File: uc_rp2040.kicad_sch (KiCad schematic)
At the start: 39 parts, among them Q6 BC817-25W, SW2 SW_B3U-1000P_SMD, SW3 SW_B3U-1000P_SMD, U8 W25Q128JVSIQ_SOIC-8, U9 RP2040

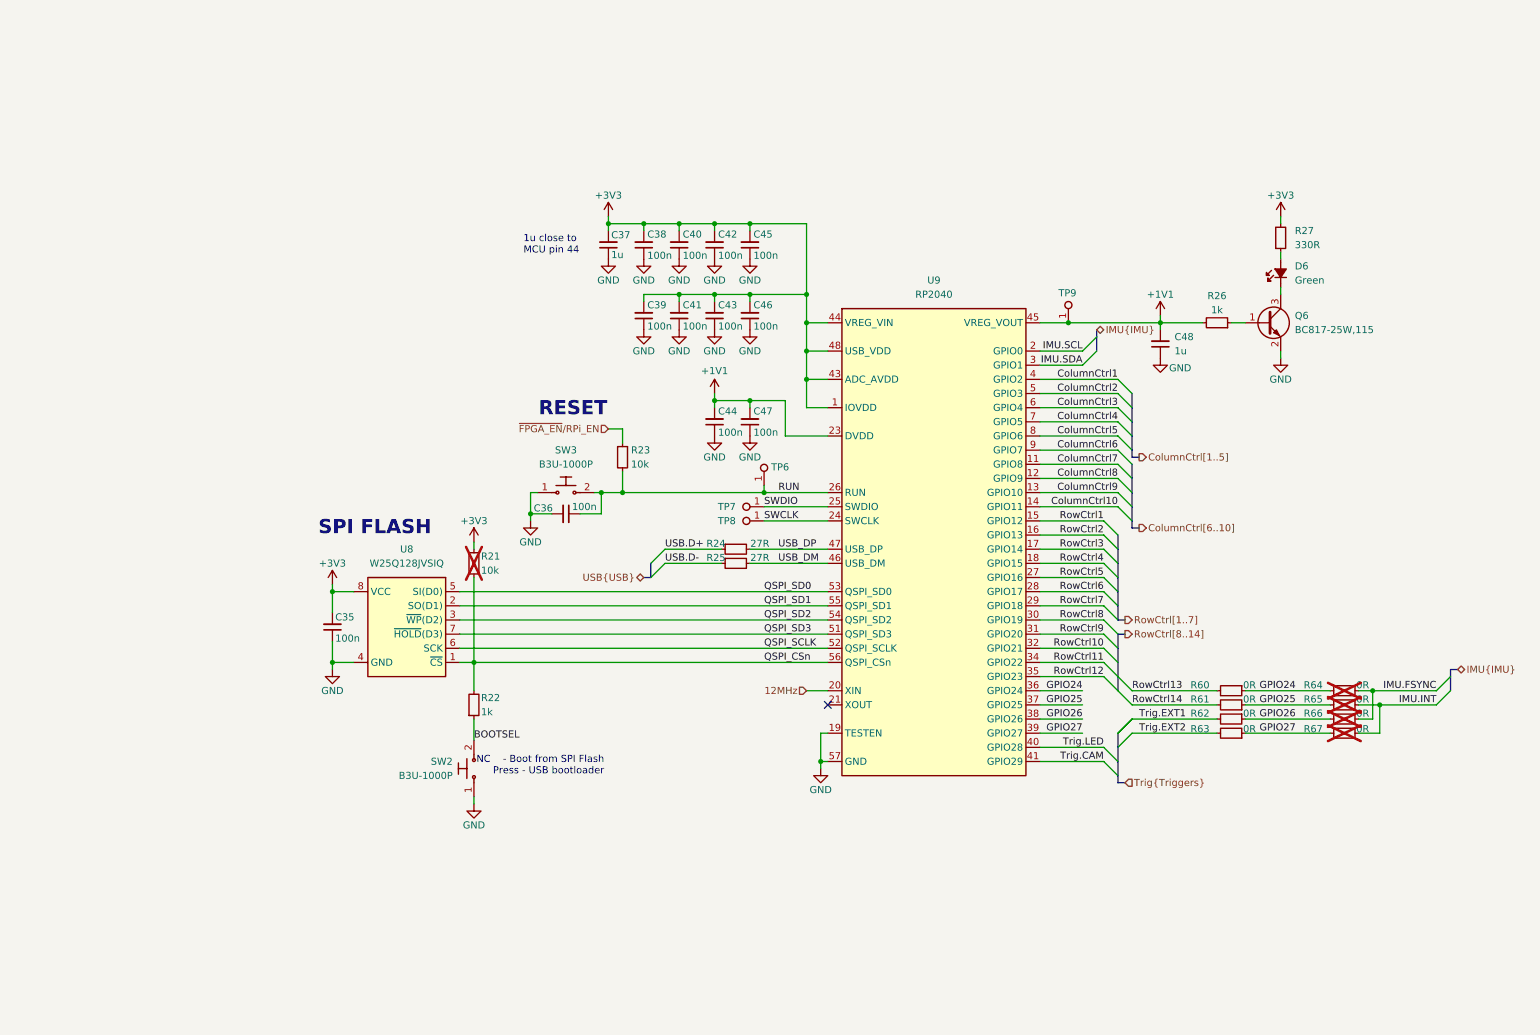
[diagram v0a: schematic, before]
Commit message: [#72133] Sch: Update control hierarchy
Signed-off-by: Dawid Lentka <dlentka@antmicro.com>
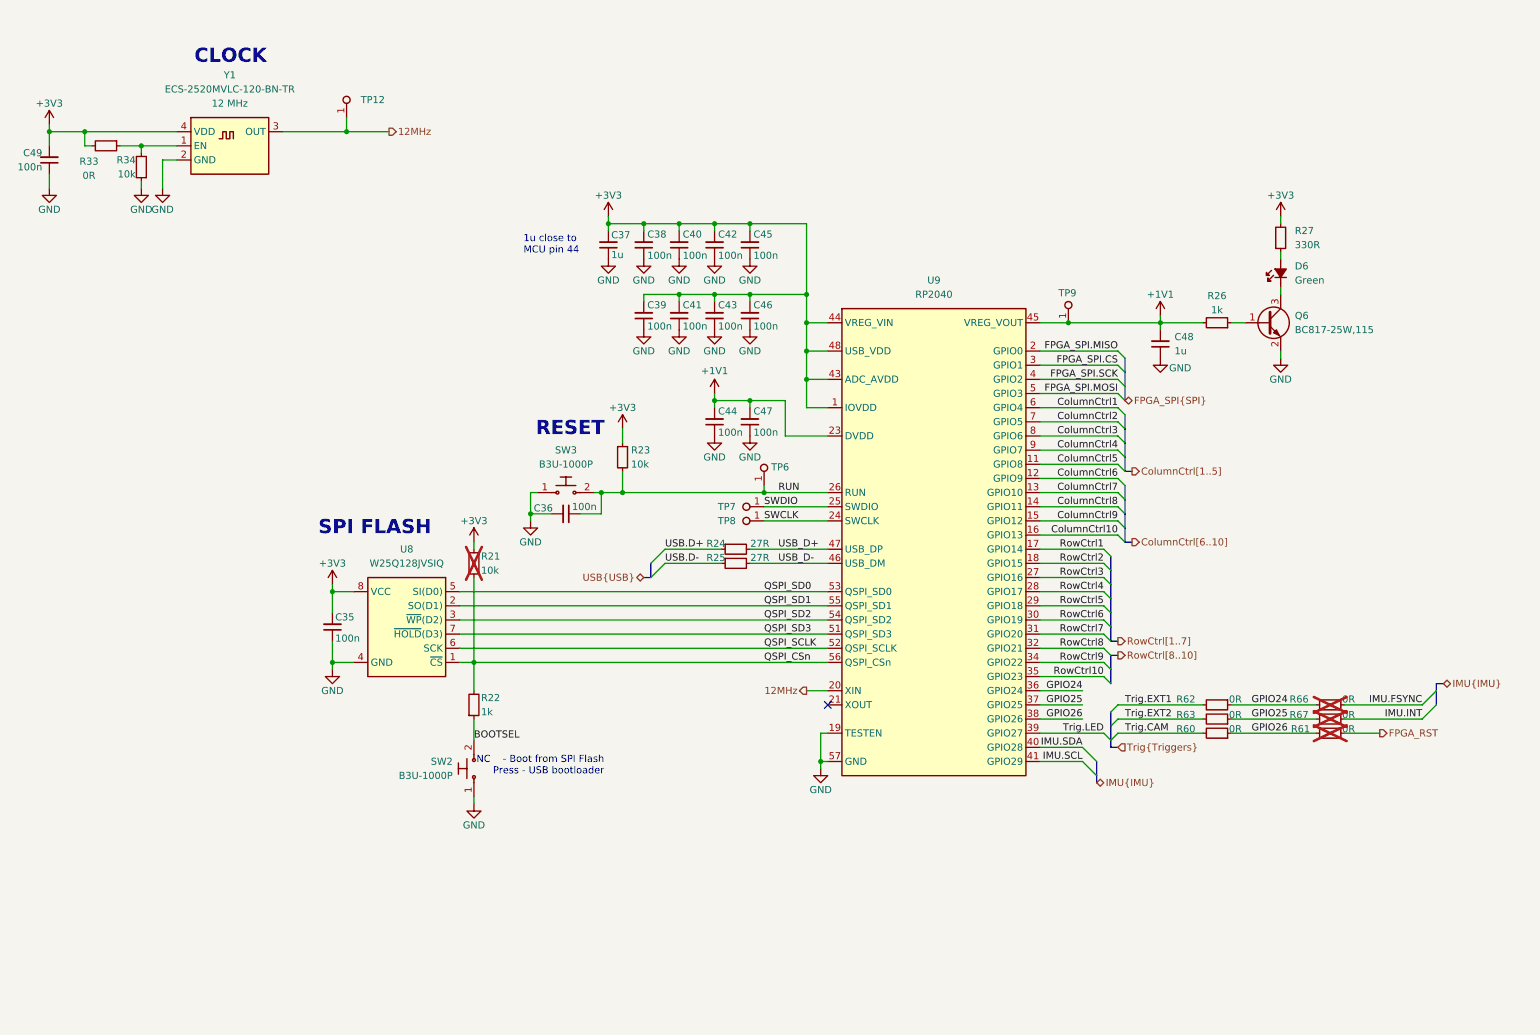
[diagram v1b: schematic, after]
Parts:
- removed R64, R65: R_0R_0402, antmicro-footprints:R_0402_1005Metric, symbol antmicroResistors0402:R_0R_0402
- added C49: C_100n_0402, antmicro-footprints:C_0402_1005Metric, symbol antmicroCapacitors0402:C_100n_0402
- added R33: R_0R_0402, antmicro-footprints:R_0402_1005Metric, symbol antmicroResistors0402:R_0R_0402
- added R34: R_10k_0402, antmicro-footprints:R_0402_1005Metric, symbol antmicroResistors0402:R_10k_0402
- added TP12: TP_0.75mm_SMD, antmicro-footprints:TP_SMD_0.75mm, symbol antmicroTestPoints:TP_0.75mm_SMD
- added Y1: Oscillator_12MHz_ESC_2520MV, antmicro-footprints:Oscillator_SMD_ECS_2520MV_2.5x2mm, symbol antmicroOscillators:Oscillator_12MHz_ESC_2520MV
- R61: now not fitted
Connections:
- net RowCtrl11 is gone; now on net RowCtrl9: U9.34 (GPIO22)
- net RowCtrl12 is gone; now on net RowCtrl10: U9.35 (GPIO23)
- net RowCtrl13 is gone; now on net Trig.CAM: R60.2
- net RowCtrl14 is gone; now on net GPIO26: R61.2
- net ~{FPGA_EN}/RPi_EN is gone; now on net +3V3: R23.1
- net +3V3: now also C49.2, R33.2, Y1.4 (VDD)
- net 12MHz: now also TP12.1, Y1.3 (OUT)
- net ColumnCtrl1: now also U9.6 (GPIO4); no longer U9.4 (GPIO2)
- net ColumnCtrl10: now also U9.16 (GPIO13); no longer U9.14 (GPIO11)
- net ColumnCtrl2: now also U9.7 (GPIO5); no longer U9.5 (GPIO3)
- net ColumnCtrl3: now also U9.8 (GPIO6); no longer U9.6 (GPIO4)
- net ColumnCtrl4: now also U9.9 (GPIO7); no longer U9.7 (GPIO5)
- net ColumnCtrl5: now also U9.11 (GPIO8); no longer U9.8 (GPIO6)
- net ColumnCtrl6: now also U9.12 (GPIO9); no longer U9.9 (GPIO7)
- net ColumnCtrl7: now also U9.13 (GPIO10); no longer U9.11 (GPIO8)
- net ColumnCtrl8: now also U9.14 (GPIO11); no longer U9.12 (GPIO9)
- net ColumnCtrl9: now also U9.15 (GPIO12); no longer U9.13 (GPIO10)
- net GND: now also C49.1, R34.1, Y1.2 (GND)
- net GPIO24: now also R62.1, R66.2; no longer R60.1
- net GPIO25: now also R63.1, R67.2; no longer R61.1
- net GPIO26: now also R60.1; no longer R62.1, R66.2
- net IMU.SCL: now also U9.41 (GPIO29); no longer U9.2 (GPIO0)
- net IMU.SDA: now also U9.40 (GPIO28); no longer U9.3 (GPIO1)
- net RowCtrl1: now also U9.17 (GPIO14); no longer U9.15 (GPIO12)
- net RowCtrl10: no longer U9.32 (GPIO21)
- net RowCtrl2: now also U9.18 (GPIO15); no longer U9.16 (GPIO13)
- net RowCtrl3: now also U9.27 (GPIO16); no longer U9.17 (GPIO14)
- net RowCtrl4: now also U9.28 (GPIO17); no longer U9.18 (GPIO15)
- net RowCtrl5: now also U9.29 (GPIO18); no longer U9.27 (GPIO16)
- net RowCtrl6: now also U9.30 (GPIO19); no longer U9.28 (GPIO17)
- net RowCtrl7: now also U9.31 (GPIO20); no longer U9.29 (GPIO18)
- net RowCtrl8: now also U9.32 (GPIO21); no longer U9.30 (GPIO19)
- net RowCtrl9: no longer U9.31 (GPIO20)
- net Trig.CAM: no longer U9.41 (GPIO29)
- net Trig.LED: now also U9.39 (GPIO27); no longer U9.40 (GPIO28)
- removed net GPIO27: R63.1, R67.2, U9.39 (GPIO27)
- net USB_DM renamed USB_D-
- net USB_DP renamed USB_D+
- new net: R33.1, R34.2, Y1.1 (EN)
- new net FPGA_RST: R61.1
- new net FPGA_SPI.CS: U9.3 (GPIO1)
- new net FPGA_SPI.MISO: U9.2 (GPIO0)
- new net FPGA_SPI.MOSI: U9.5 (GPIO3)
- new net FPGA_SPI.SCK: U9.4 (GPIO2)
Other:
- note added: "CLOCK"
- moved on the sheet: R62, R63, R66, R67

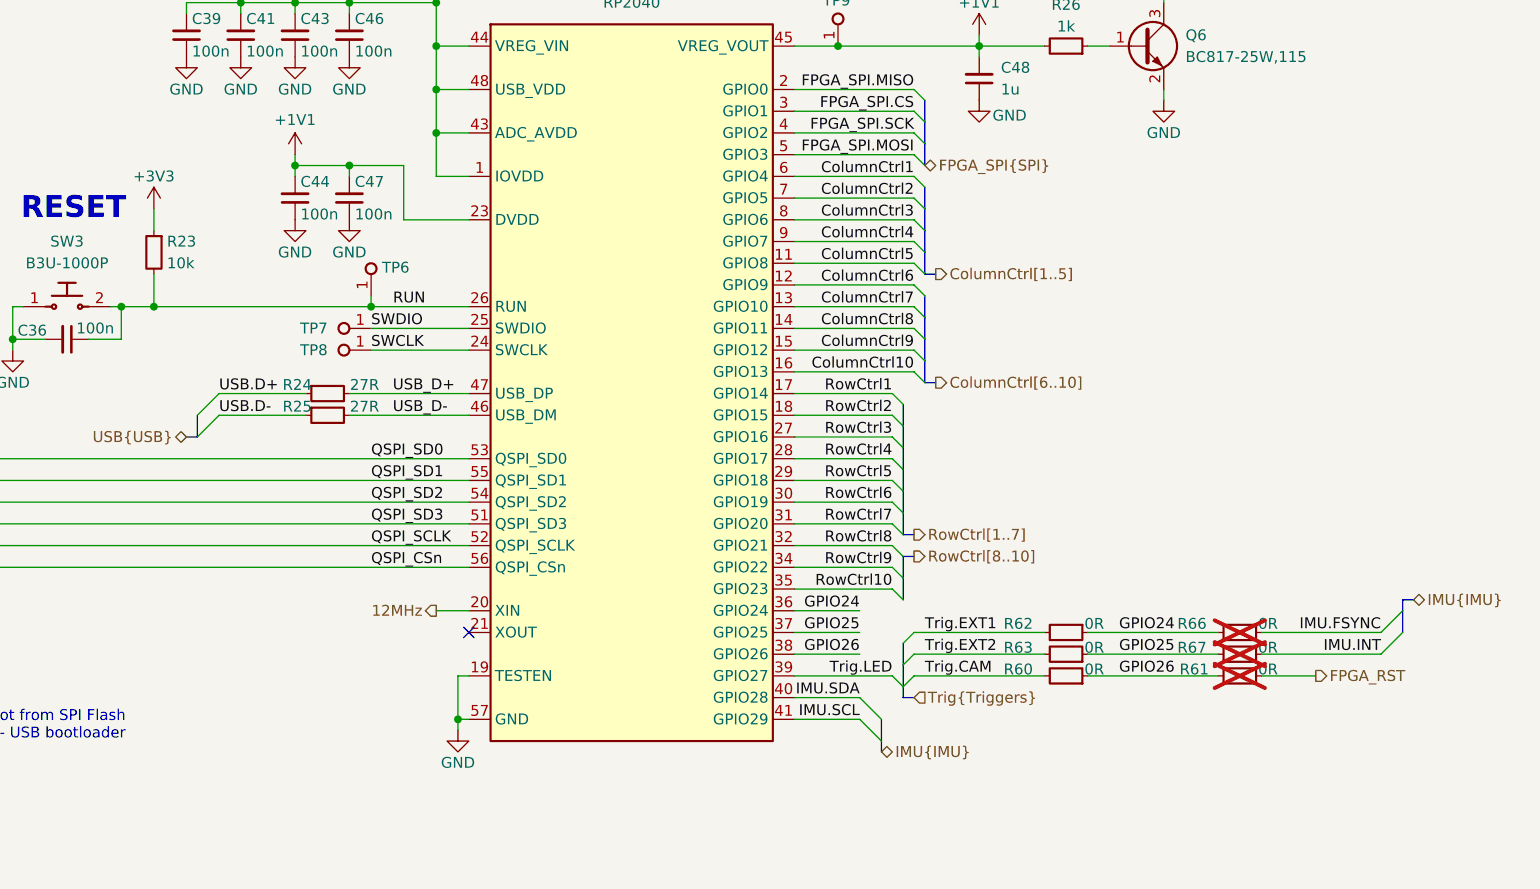
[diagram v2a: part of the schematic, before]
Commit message: [#72133] Update USB FTDI sheet
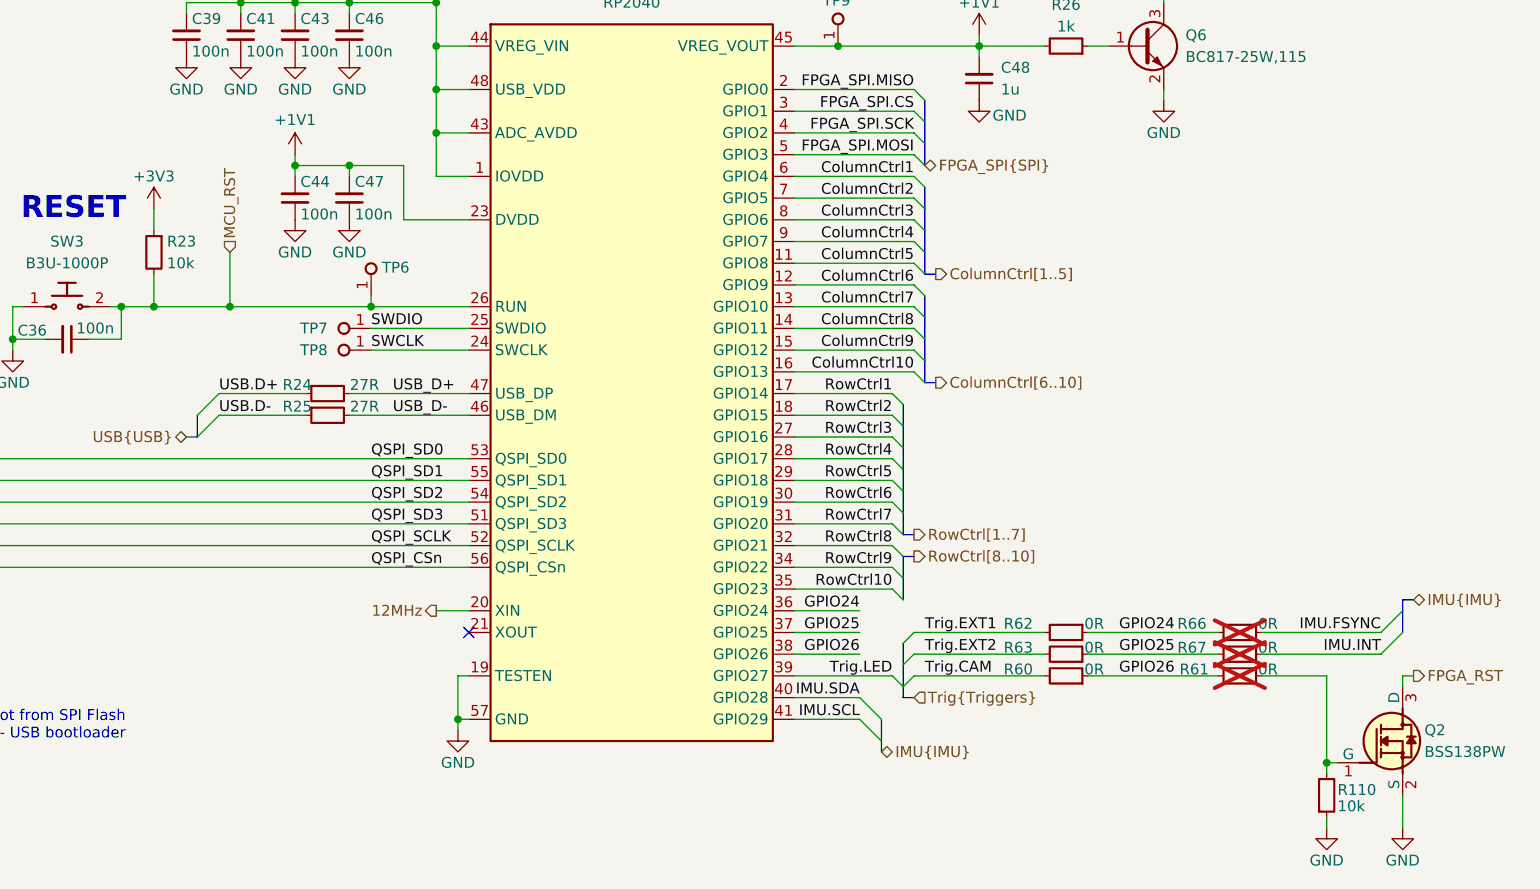
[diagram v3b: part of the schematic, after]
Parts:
- added Q2: BSS138PW, antmicro-footprints:SC70-3, symbol antmicroTransistorsFETsMOSFETsSingle:BSS138PW
- added R110: R_10k_0402, antmicro-footprints:R_0402_1005Metric, symbol antmicroResistors0402:R_10k_0402
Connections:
- net FPGA_RST: now also Q2.3 (D); no longer R61.1
- net GND: now also Q2.2 (S), R110.1
- net RUN renamed MCU_RST
- new net: Q2.1 (G), R110.2, R61.1

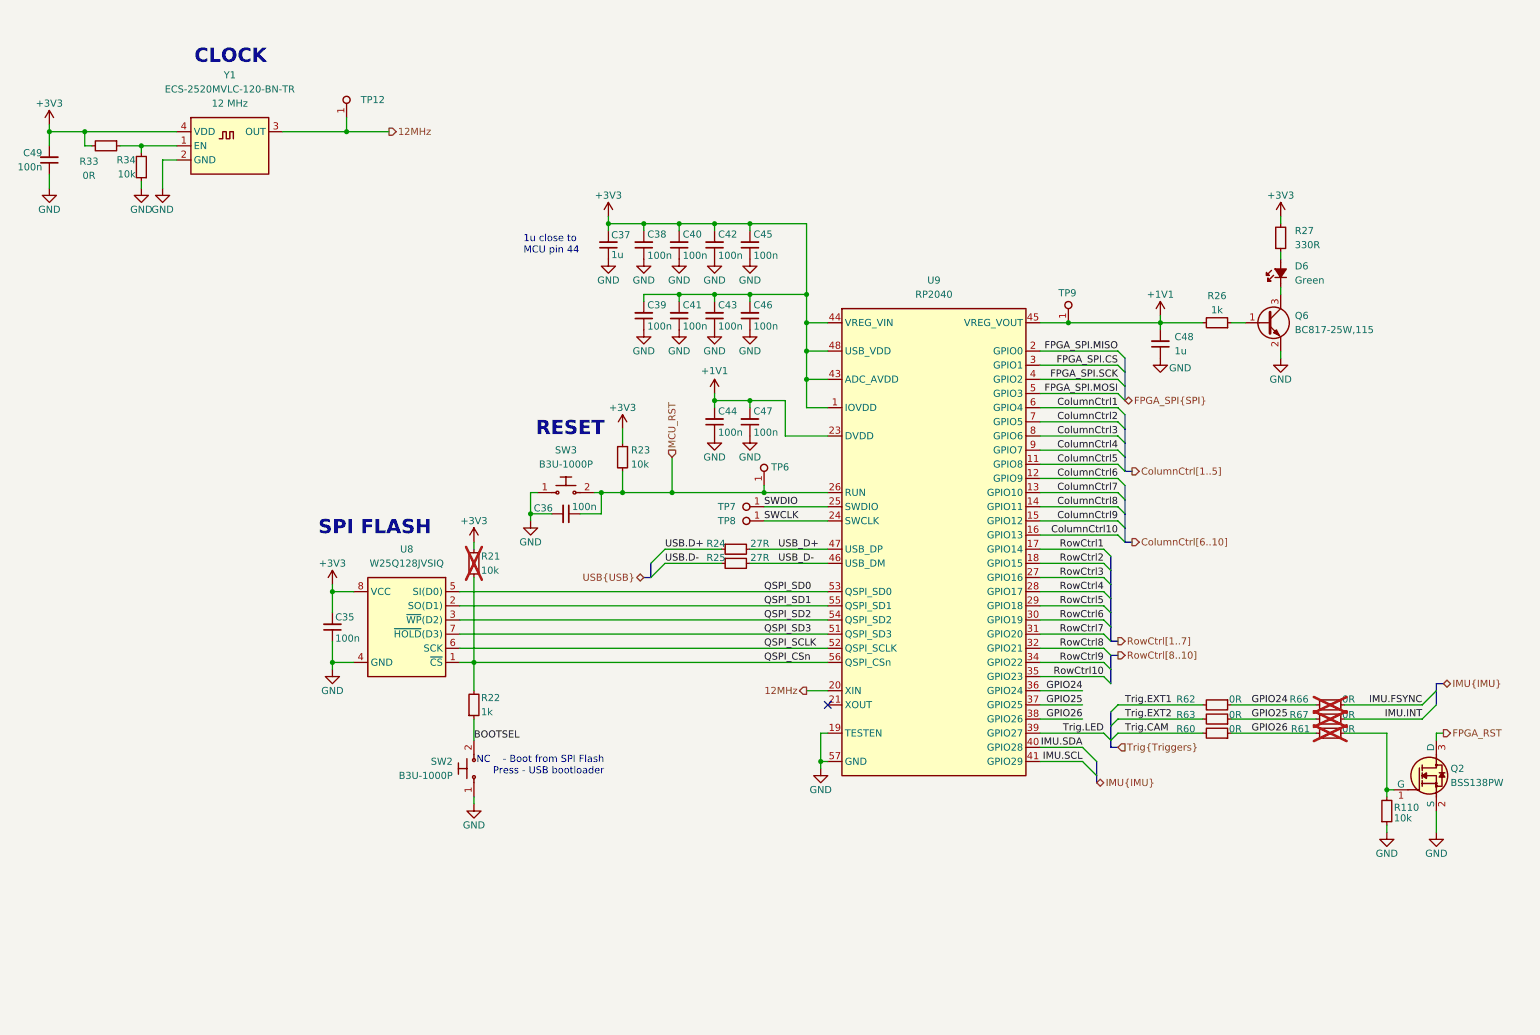
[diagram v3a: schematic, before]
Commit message: [#72133] Add captions to schematic sheets
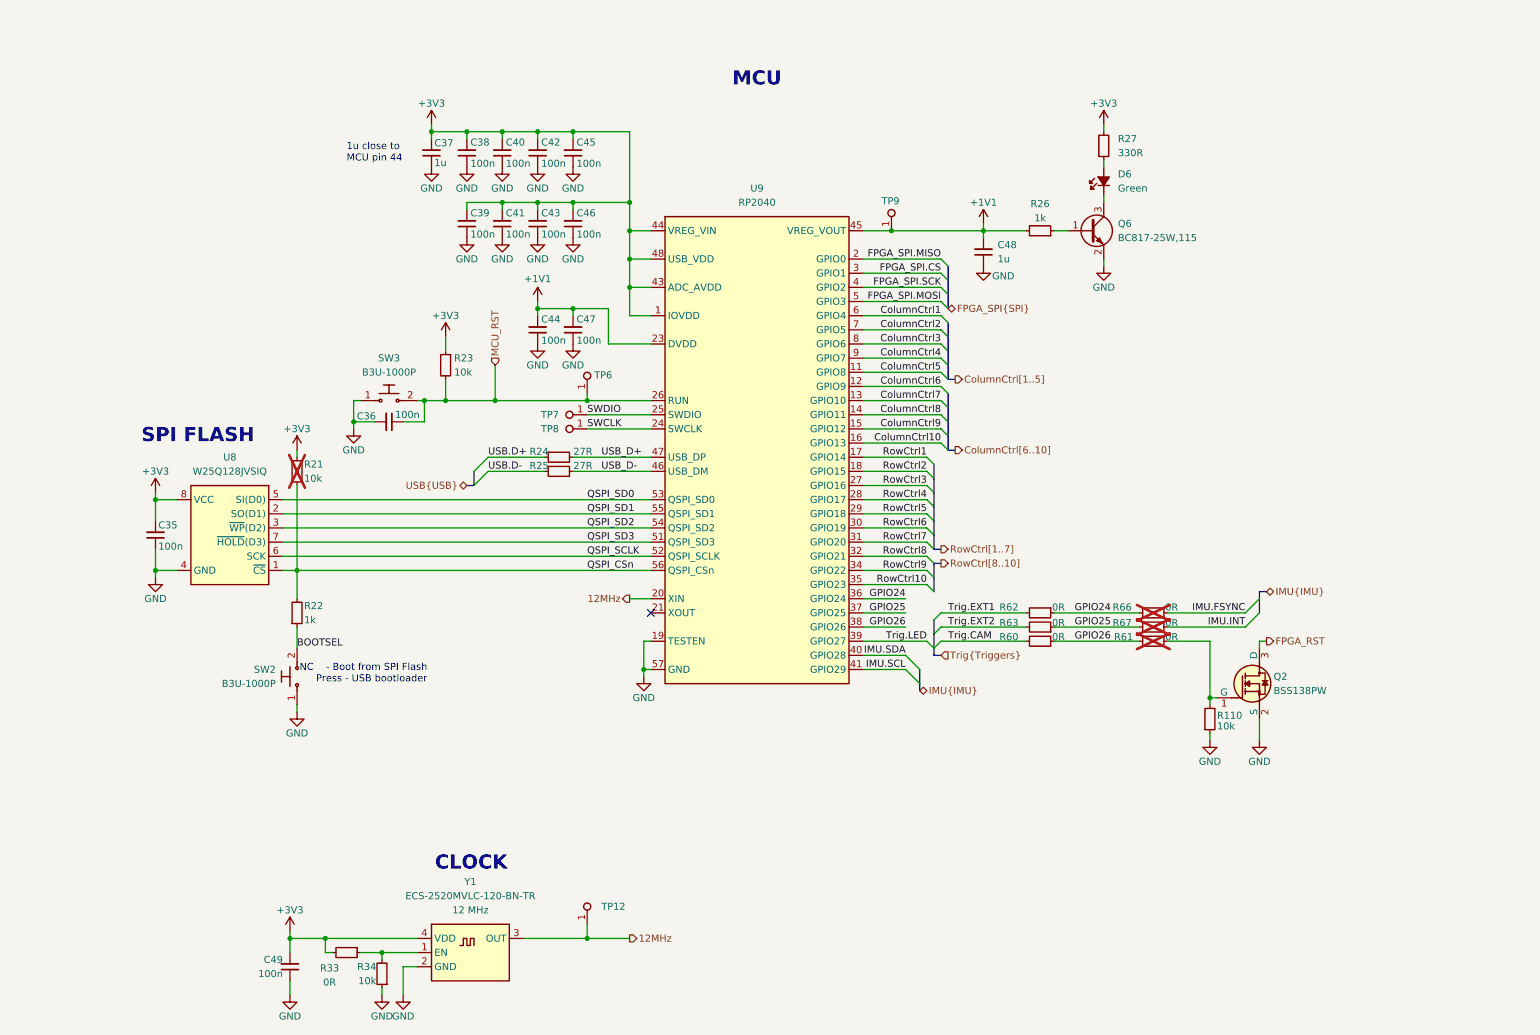
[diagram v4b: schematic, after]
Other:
- note added: "MCU"
- note removed: "RESET"
- moved on the sheet: C35, C36, C37, C38, C39, C40, C41, C42, C43, C44, C45, C46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
